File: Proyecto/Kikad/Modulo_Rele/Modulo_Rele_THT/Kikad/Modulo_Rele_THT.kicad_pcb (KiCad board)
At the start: 2 copper layers, 52.7 x 20.3 mm, 9 parts, among them J1 TB_1X3, J2 TB_1X3, K1 RELAY_C, Q1 BC337, U3 PC817

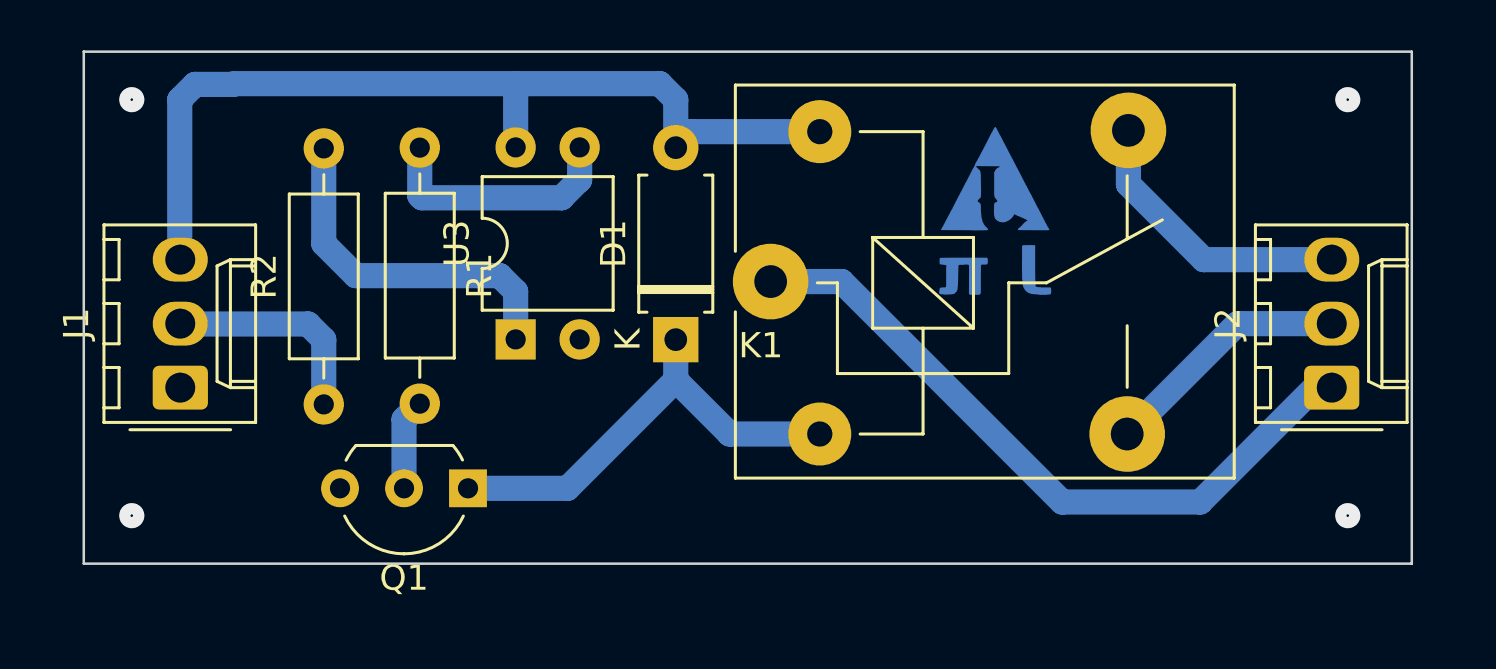
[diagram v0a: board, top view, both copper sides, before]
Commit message: hice el Rele Mixto y adjunte sus imagenes. ademas agregue la resistencia de 10K
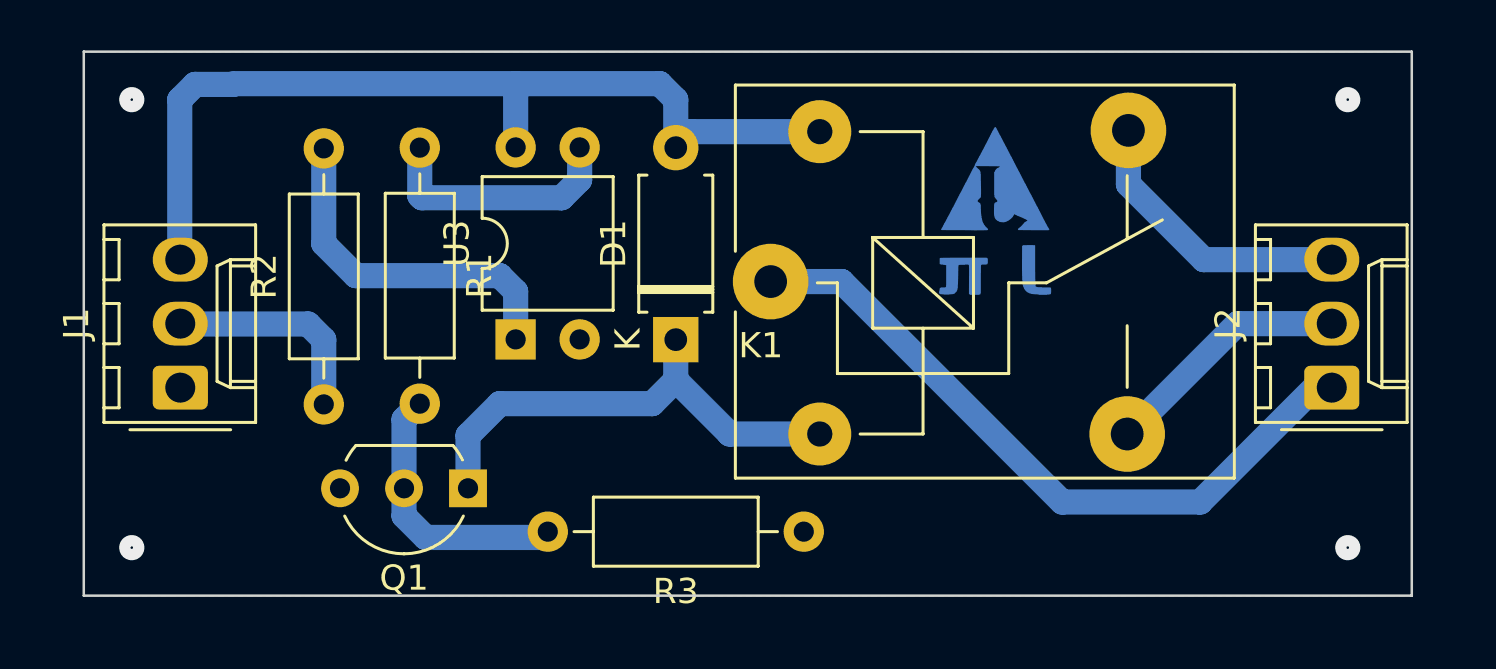
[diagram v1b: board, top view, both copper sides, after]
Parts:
- added R3: 10K, Resistor_THT:R_Axial_DIN0207_L6.3mm_D2.5mm_P10.16mm_Horizontal, F.Cu at (138.4, 125.7)
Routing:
- net Net-(Q1-B): track 3.62 -> 10.9 mm
- net Net-(D1-A): track 18.2 -> 19.5 mm
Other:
- board size 52.7 x 20.3 mm -> 52.7 x 21.6 mm

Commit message: Agregue la carpeta Placa_Principal e hice unas correcciones en el Modulo_Rele
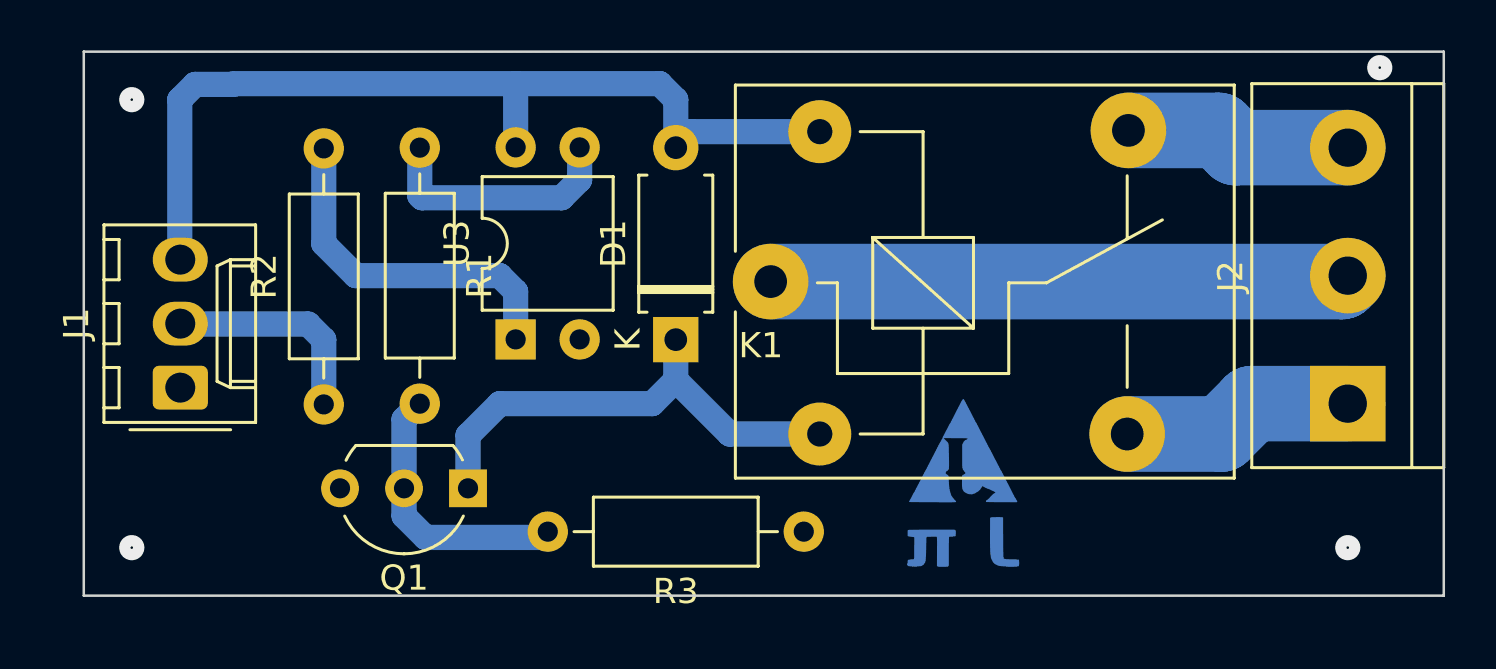
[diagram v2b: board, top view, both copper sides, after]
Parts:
- J2: footprint Connector_Molex:Molex_KK-254_AE-6410-03A_1x03_P2.54mm_Vertical -> TerminalBlock:TerminalBlock_bornier-3_P5.08mm
- R2: value 220 -> 470
- moved G*** 10.9 mm to (144.8, 123.8)
- moved J2 0.90 mm to (160.0, 120.7)
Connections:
- K1 pad 1: Net-(J2-Pad1) -> Net-(J2-Pad2)
- K1 pad 3: Net-(J2-Pad2) -> Net-(J2-Pad1)
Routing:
- net Net-(J2-Pad1): track 27.1 -> 9.25 mm
- net Net-(J2-Pad2): track 9.25 -> 23.0 mm
- net Net-(J2-Pad3): track 10.8 -> 8.99 mm
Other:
- board size 52.7 x 21.6 mm -> 54 x 21.6 mm
